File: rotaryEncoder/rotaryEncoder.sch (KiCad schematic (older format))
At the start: 12 parts, among them J1 Select

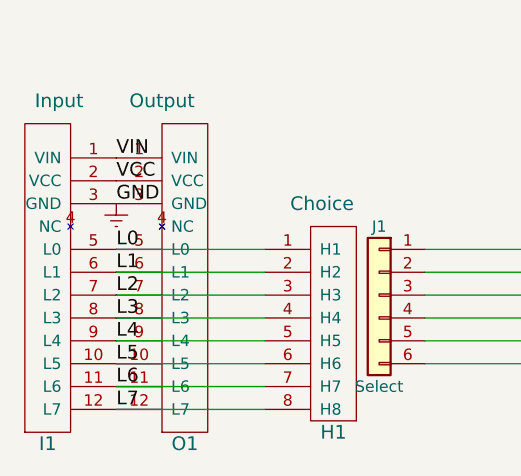
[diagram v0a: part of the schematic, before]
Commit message: More update to make the libraryies use only relative paths.
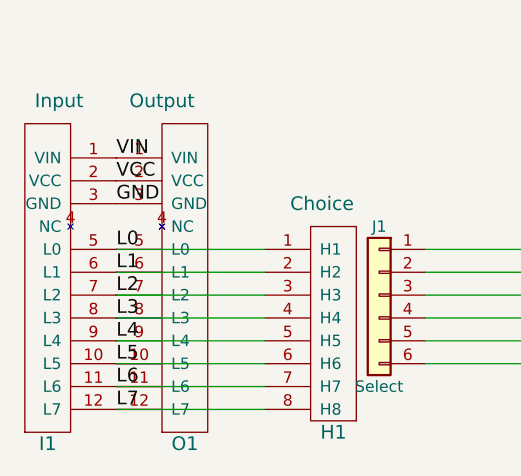
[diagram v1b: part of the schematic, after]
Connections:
- net Earth renamed GND
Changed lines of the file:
@@
 LIBS:valves
 LIBS:eplay
-LIBS:Rotary-Encoders
 LIBS:rotaryEncoder-cache
 EELAYER 25 0
@@
 L7
 $Comp
-L Earth #PWR1
-U 1 1 5AC24527
-P 2250 2100
-F 0 "#PWR1" H 2250 1850 50  0001 C CNN
-F 1 "Earth" H 2250 1950 50  0001 C CNN
-F 2 "" H 2250 2100 50  0001 C CNN
-F 3 "" H 2250 2100 50  0001 C CNN
-	1    2250 2100
-	1    0    0    -1
-$EndComp
-$Comp
 L Input I1
